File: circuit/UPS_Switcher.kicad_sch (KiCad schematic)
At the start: 19 parts, among them K1 HK4100F, M1 Motor_Servo, Q1 AO3400A, Q2 AO3400A, U1 L79L05_TO92

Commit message: Небольшие исправления на схеме.
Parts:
- added R7: 1M, symbol Device:R
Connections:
- net N: now also R7.2; no longer NE1.1
- new net: NE1.1, R7.1
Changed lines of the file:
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@@
 	(wire
 		(pts
-			(xy 50.8 157.48) (xy 50.8 162.56)
-		)
-		(stroke
-			(width 0)
-			(type default)
-		)
-	)
-	(wire
-		(pts
-			(xy 80.01 160.02) (xy 80.01 170.18)
+			(xy 80.01 160.02) (xy 80.01 167.64)
 		)
 		(stroke
@@
 	(wire
 		(pts
-			(xy 29.21 165.1) (xy 29.21 171.45)
+			(xy 29.21 165.1) (xy 29.21 167.64)
 		)
 		(stroke
@@
 	(wire
 		(pts
-			(xy 124.46 143.51) (xy 124.46 171.45)
+			(xy 124.46 143.51) (xy 124.46 168.91)
 		)
 		(stroke
@@
 	(wire
 		(pts
-			(xy 124.46 171.45) (xy 132.08 171.45)
+			(xy 124.46 168.91) (xy 132.08 168.91)
 		)
 		(stroke
@@
 	(wire
 		(pts
-			(xy 173.99 20.32) (xy 173.99 30.48)
+			(xy 173.99 21.59) (xy 173.99 30.48)
 		)
 		(stroke
@@
 		(pts
 			(xy 77.47 46.99) (xy 77.47 62.23)
+		)
+		(stroke
+			(width 0)
+			(type default)
+		)
+	)
+	(wire
+		(pts
+			(xy 50.8 168.91) (xy 50.8 171.45)
+		)
+		(stroke
+			(width 0)
+			(type default)
+		)
+	)
+	(wire
+		(pts
+			(xy 50.8 157.48) (xy 50.8 161.29)
 		)
 		(stroke
@@
 	(global_label "COMP_STAT"
 		(shape output)
-		(at 132.08 171.45 0)
+		(at 132.08 168.91 0)
 		(fields_autoplaced yes)
 		(effects
@@
 		)
 		(property "Intersheetrefs" "${INTERSHEET_REFS}"
-			(at 145.588 171.45 0)
+			(at 145.588 168.91 0)
 			(effects
 				(font
@@
 	(symbol
 		(lib_id "power:+BATT")
-		(at 173.99 20.32 0)
+		(at 173.99 21.59 0)
 		(unit 1)
 		(exclude_from_sim no)
@@
 		(fields_autoplaced yes)
 		(property "Reference" "#PWR04"
-			(at 173.99 24.13 0)
+			(at 173.99 25.4 0)
 			(effects
 				(font
@@
 		)
 		(property "Value" "+6V (BATT)"
-			(at 173.99 15.24 0)
+			(at 173.99 16.51 0)
 			(effects
 				(font
@@
 		)
 		(property "Footprint" ""
-			(at 173.99 20.32 0)
+			(at 173.99 21.59 0)
 			(effects
 				(font
@@
 		)
 		(property "Datasheet" ""
-			(at 173.99 20.32 0)
+			(at 173.99 21.59 0)
 			(effects
 				(font
@@
 		)
 		(property "Description" "Power symbol creates a global label with name \"+BATT\""
-			(at 173.99 20.32 0)
+			(at 173.99 21.59 0)
 			(effects
 				(font
@@
 	(symbol
 		(lib_id "power:GNDREF")
-		(at 80.01 170.18 0)
+		(at 80.01 167.64 0)
 		(unit 1)
 		(exclude_from_sim no)
@@
 		(fields_autoplaced yes)
 		(property "Reference" "#PWR08"
-			(at 80.01 176.53 0)
+			(at 80.01 173.99 0)
 			(effects
 				(font
@@
 		)
 		(property "Value" "GND"
-			(at 80.01 175.26 0)
+			(at 80.01 172.72 0)
 			(effects
 				(font
@@
 		)
 		(property "Footprint" ""
-			(at 80.01 170.18 0)
+			(at 80.01 167.64 0)
 			(effects
 				(font
@@
 		)
 		(property "Datasheet" ""
-			(at 80.01 170.18 0)
+			(at 80.01 167.64 0)
 			(effects
 				(font
@@
 		)
 		(property "Description" "Power symbol creates a global label with name \"GNDREF\" , reference supply ground"
-			(at 80.01 170.18 0)
+			(at 80.01 167.64 0)
 			(effects
 				(font
@@
 				(path "/c004cbc3-9abe-49e6-8c82-c59412dd127a"
 					(reference "#PWR08")
+					(unit 1)
+				)
+			)
+		)
+	)
+	(symbol
+		(lib_id "Device:R")
+		(at 50.8 165.1 0)
+		(unit 1)
+		(exclude_from_sim no)
+		(in_bom yes)
+		(on_board yes)
+		(dnp no)
+		(fields_autoplaced yes)
+		(property "Reference" "R7"
+			(at 53.34 163.8299 0)
+			(effects
+				(font
+					(size 1.27 1.27)
+				)
+				(justify left)
+			)
+		)
+		(property "Value" "1M"
+			(at 53.34 166.3699 0)
+			(effects
+				(font
+					(size 1.27 1.27)
+				)
+				(justify left)
+			)
+		)
+		(property "Footprint" ""
+			(at 49.022 165.1 90)
+			(effects
+				(font
+					(size 1.27 1.27)
+				)
+				(hide yes)
+			)
+		)
+		(property "Datasheet" "~"
+			(at 50.8 165.1 0)
+			(effects
+				(font
+					(size 1.27 1.27)
+				)
+				(hide yes)
+			)
+		)
+		(property "Description" "Resistor"
+			(at 50.8 165.1 0)
+			(effects
+				(font
+					(size 1.27 1.27)
+				)
+				(hide yes)
+			)
+		)
+		(pin "1"
+		)
+		(pin "2"
+		)
+		(instances
+			(project "UPS_Switcher"
+				(path "/c004cbc3-9abe-49e6-8c82-c59412dd127a"
+					(reference "R7")
 					(unit 1)
 				)
@@
 	(symbol
 		(lib_id "power:GNDREF")
-		(at 29.21 171.45 0)
+		(at 29.21 167.64 0)
 		(unit 1)
 		(exclude_from_sim no)
@@
 		(fields_autoplaced yes)
 		(property "Reference" "#PWR03"
-			(at 29.21 177.8 0)
+			(at 29.21 173.99 0)
 			(effects
 				(font
@@
 		)
 		(property "Value" "GND"
-			(at 29.21 176.53 0)
+			(at 29.21 172.72 0)
 			(effects
 				(font
@@
 		)
 		(property "Footprint" ""
-			(at 29.21 171.45 0)
+			(at 29.21 167.64 0)
 			(effects
 				(font
@@
 		)
 		(property "Datasheet" ""
-			(at 29.21 171.45 0)
+			(at 29.21 167.64 0)
 			(effects
 				(font
@@
 		)
 		(property "Description" "Power symbol creates a global label with name \"GNDREF\" , reference supply ground"
-			(at 29.21 171.45 0)
+			(at 29.21 167.64 0)
 			(effects
 				(font
@@
 	(symbol
 		(lib_id "power:NEUT")
-		(at 50.8 162.56 180)
+		(at 50.8 171.45 180)
 		(unit 1)
 		(exclude_from_sim no)
@@
 		(fields_autoplaced yes)
 		(property "Reference" "#PWR06"
-			(at 50.8 158.75 0)
+			(at 50.8 167.64 0)
 			(effects
 				(font
@@
 		)
 		(property "Value" "N"
-			(at 50.8 167.64 0)
+			(at 50.8 176.53 0)
 			(effects
 				(font
@@
 		)
 		(property "Footprint" ""
-			(at 50.8 162.56 0)
+			(at 50.8 171.45 0)
 			(effects
 				(font
@@
 		)
 		(property "Datasheet" ""
-			(at 50.8 162.56 0)
+			(at 50.8 171.45 0)
 			(effects
 				(font
@@
 		)
 		(property "Description" "Power symbol creates a global label with name \"NEUT\""
-			(at 50.8 162.56 0)
-			(effects
-				(font
+			(at 50.8 171.45 0)
+			(effects
+				(font

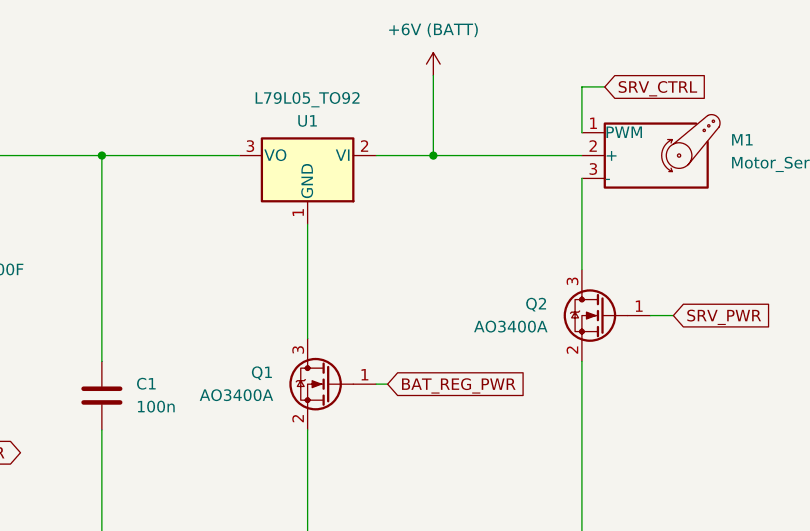
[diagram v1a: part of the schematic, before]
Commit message: Добавил недостающий конденсатор.
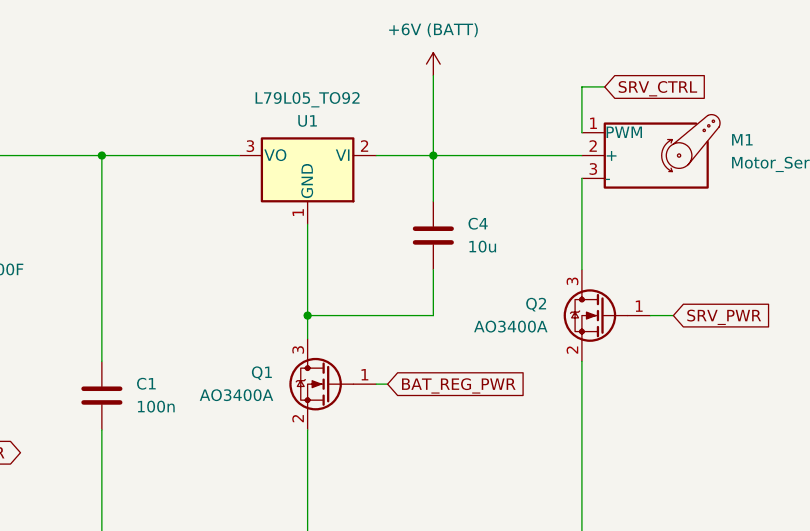
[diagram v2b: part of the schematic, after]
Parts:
- added C4: 10u, symbol Device:C
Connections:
- net +6V (BATT): now also C4.1
- net at Q1.3 (D), U1.1 (GND): now also C4.2
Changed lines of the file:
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@@
+	)
+	(junction
+		(at 160.02 48.26)
+		(diameter 0)
+		(color 0 0 0 0)
 	)
 	(junction
@@
 	(wire
 		(pts
+			(xy 160.02 48.26) (xy 160.02 50.8)
+		)
+		(stroke
+			(width 0)
+			(type default)
+		)
+	)
+	(wire
+		(pts
 			(xy 168.91 55.88) (xy 167.64 55.88)
 		)
@@
 	(wire
 		(pts
-			(xy 160.02 38.1) (xy 160.02 50.8)
+			(xy 160.02 38.1) (xy 160.02 48.26)
 		)
 		(stroke
@@
 	(wire
 		(pts
+			(xy 173.99 30.48) (xy 173.99 35.56)
+		)
+		(stroke
+			(width 0)
+			(type default)
+		)
+	)
+	(wire
+		(pts
 			(xy 77.47 69.85) (xy 77.47 76.2)
 		)
@@
 	(wire
 		(pts
+			(xy 173.99 48.26) (xy 160.02 48.26)
+		)
+		(stroke
+			(width 0)
+			(type default)
+		)
+	)
+	(wire
+		(pts
 			(xy 114.3 76.2) (xy 114.3 81.28)
 		)
@@
 		(pts
 			(xy 36.83 134.62) (xy 36.83 148.59)
+		)
+		(stroke
+			(width 0)
+			(type default)
+		)
+	)
+	(wire
+		(pts
+			(xy 173.99 43.18) (xy 173.99 48.26)
 		)
 		(stroke
@@
 					(unit 1)
 				)
+			)
+		)
+	)
+	(symbol
+		(lib_id "Device:C")
+		(at 173.99 39.37 0)
+		(unit 1)
+		(exclude_from_sim no)
+		(in_bom yes)
+		(on_board yes)
+		(dnp no)
+		(fields_autoplaced yes)
+		(property "Reference" "C4"
+			(at 177.8 38.0999 0)
+			(effects
+				(font
+					(size 1.27 1.27)
+				)
+				(justify left)
+			)
+		)
+		(property "Value" "10u"
+			(at 177.8 40.6399 0)
+			(effects
+				(font
+					(size 1.27 1.27)
+				)
+				(justify left)
+			)
+		)
+		(property "Footprint" ""
+			(at 174.9552 43.18 0)
+			(effects
+				(font
+					(size 1.27 1.27)
+				)
+				(hide yes)
+			)
+		)
+		(property "Datasheet" "~"
+			(at 173.99 39.37 0)
+			(effects
+				(font
+					(size 1.27 1.27)
+				)
+				(hide yes)
+			)
+		)
+		(property "Description" "Unpolarized capacitor"
+			(at 173.99 39.37 0)
+			(effects
+				(font
+					(size 1.27 1.27)
+				)
+				(hide yes)
+			)
+		)
+		(pin "1"
+		)
+		(pin "2"
+		)
+		(instances
+			(project "UPS_Switcher"
+				(path "/c004cbc3-9abe-49e6-8c82-c59412dd127a"
+					(reference "C4")
+					(unit 1)
+				)

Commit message: Небольшие правки схемы
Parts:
- R7: value 1M -> 470K
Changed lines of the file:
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@@
 			)
 		)
-		(property "Value" "1M"
+		(property "Value" "470K"
 			(at 53.34 166.3699 0)
 			(effects
